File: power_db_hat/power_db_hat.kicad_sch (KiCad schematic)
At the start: 32 parts, among them J2 BAT2, J5 24V_out, J8 BAT1, U7 B2B pins

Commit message: lol
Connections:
- net +3V3: now also U7.5c, U7.7c; no longer U7.8c
- net GND: now also U7.11c, U7.9c; no longer U7.10c, U7.12c
- net LED_PWM_1: now also U7.12c; no longer U7.9c
- net LED_PWM_2: now also U7.10c; no longer U7.11c
- net MOTOR_1_A: now also U7.8c; no longer U7.1c
- net MOTOR_1_B: now also U7.6c; no longer U7.3c
- net MOTOR_2_A: now also U7.4c; no longer U7.5c
- net MOTOR_2_B: now also U7.2c; no longer U7.7c
- net SERVO_1: now also U7.3c; no longer U7.2c
- net SERVO_2: now also U7.1c; no longer U7.4c
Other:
- moved on the sheet: C45, C46, U7C

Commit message: damo was here
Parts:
- removed C2, C4, C49: 100nF, Capacitor_SMD:C_0603_1608Metric_Pad1.08x0.95mm_HandSolder, symbol Device:C
- removed C50: 22uF, Capacitor_SMD:C_0603_1608Metric_Pad1.08x0.95mm_HandSolder, symbol Device:C
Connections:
- net GND: no longer U7.11c
- net I2C_SCL: now also U7.11b; no longer U7.12b
- net I2C_SDA: now also U7.12b; no longer U7.11b
- net IND: now also U7.11c
- net LED_PWM_1: now also U7.10c; no longer U7.12c
- net LED_PWM_2: now also U7.12c; no longer U7.10c
- net MOTOR_1_A: now also U7.4c; no longer U7.8c
- net MOTOR_1_B: now also U7.2c; no longer U7.6c
- net MOTOR_2_A: now also U7.8c; no longer U7.4c
- net MOTOR_2_B: now also U7.6c; no longer U7.2c

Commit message: working on interface board
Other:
- moved on the sheet: C45, C46, U7A, U7C

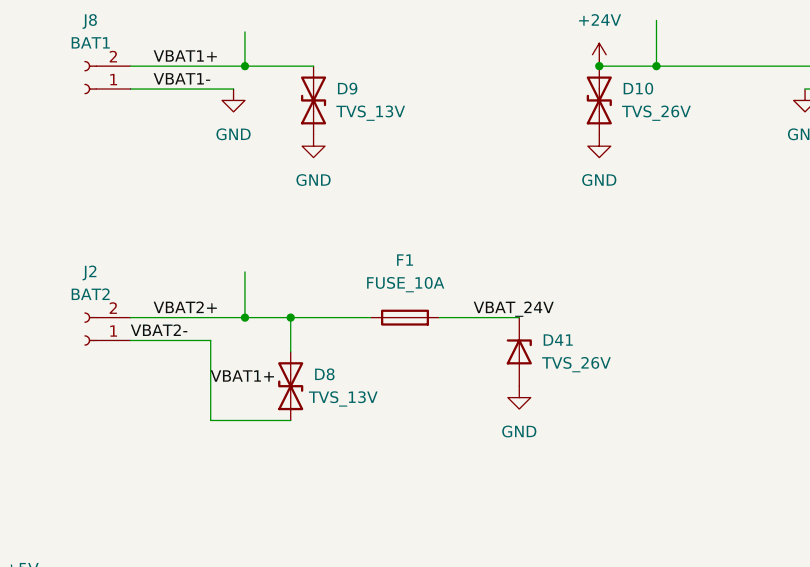
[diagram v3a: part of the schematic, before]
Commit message: updated 3d models for power
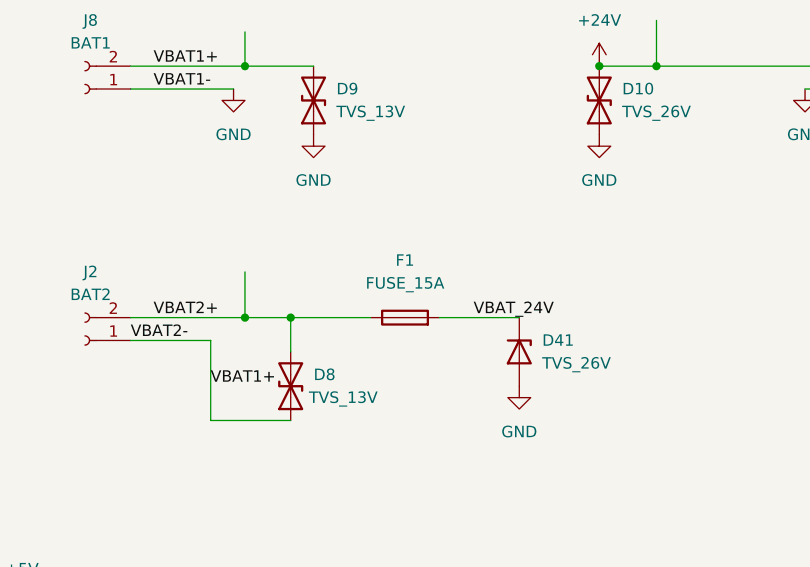
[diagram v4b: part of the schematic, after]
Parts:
- F1: value FUSE_10A -> FUSE_15A; footprint Fuse:Fuse_2512_6332Metric_Pad1.52x3.35mm_HandSolder -> Fuse:Fuse_1206_3216Metric_Pad1.42x1.75mm_HandSolder
- TP4: footprint TestPoint:TestPoint_Pad_D1.0mm -> INA3221:QFN65P400X400X100-17N-D
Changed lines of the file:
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@@
 			)
 		)
-		(property "Footprint" "TestPoint:TestPoint_Pad_D1.0mm"
+		(property "Footprint" "INA3221:QFN65P400X400X100-17N-D"
 			(at 78.74 156.21 0)
 			(hide yes)
@@
 			)
 		)
-		(property "Value" "FUSE_10A"
+		(property "Value" "FUSE_15A"
 			(at 161.29 57.15 90)
 			(show_name no)
@@
 			)
 		)
-		(property "Footprint" "Fuse:Fuse_2512_6332Metric_Pad1.52x3.35mm_HandSolder"
+		(property "Footprint" "Fuse:Fuse_1206_3216Metric_Pad1.42x1.75mm_HandSolder"
 			(at 161.29 62.738 90)
 			(hide yes)

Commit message: complete BOM
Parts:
- removed D8: TVS_13V, Diode_SMD:D_SMB_Handsoldering, symbol Device:D_TVS
- D10, D9: footprint Diode_SMD:D_SMB_Handsoldering -> Diode_SMD:D_SMA_Handsoldering
- D41: footprint Diode_SMD:D_0603_1608Metric_Pad1.05x0.95mm_HandSolder -> Diode_SMD:D_SMA_Handsoldering
- TP4: footprint INA3221:QFN65P400X400X100-17N-D -> TestPoint:TestPoint_Pad_D1.0mm
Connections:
- net VBAT2+: now also D41.1 (K)
- net VBAT_24V: no longer D41.1 (K)
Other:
- moved on the sheet: D41

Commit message: ordered
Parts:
- C46, C48: footprint Capacitor_SMD:C_0603_1608Metric_Pad1.08x0.95mm_HandSolder -> Capacitor_SMD:C_0805_2012Metric
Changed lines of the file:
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@@
 			)
 		)
-		(property "Footprint" "Capacitor_SMD:C_0603_1608Metric_Pad1.08x0.95mm_HandSolder"
+		(property "Footprint" "Capacitor_SMD:C_0805_2012Metric"
 			(at 268.9352 124.46 0)
 			(hide yes)
@@
 			)
 		)
-		(property "Footprint" "Capacitor_SMD:C_0603_1608Metric_Pad1.08x0.95mm_HandSolder"
+		(property "Footprint" "Capacitor_SMD:C_0805_2012Metric"
 			(at 201.6252 114.3 0)
 			(hide yes)

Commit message: bringup updates
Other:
- note added: "SDA AND SCL FLIPPED IN FIRST REVISION"
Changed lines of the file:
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@@
 		(date "15 nov 2012")
+	)
+	(text "SDA AND SCL FLIPPED IN FIRST REVISION\n"
+		(exclude_from_sim no)
+		(at 46.99 120.142 0)
+		(effects
+			(font
+				(size 1.27 1.27)
+			)
+		)
 	)
 	(text "TODO \ncheck available components in lab\n"
@@
 		)
 	)
-	(label "I2C_SCL"
-		(at 67.31 110.49 180)
-		(effects
-			(font
-				(size 1.27 1.27)
-			)
-			(justify right bottom)
-		)
-	)
 	(label "LED_PWM_1"
 		(at 236.22 119.38 180)
@@
 		)
 	)
+	(label "I2C_SCL"
+		(at 67.31 107.95 180)
+		(effects
+			(font
+				(size 1.27 1.27)
+			)
+			(justify right bottom)
+		)
+	)
 	(label "MOTOR_2_A"
 		(at 241.3 59.69 180)
@@
 		)
 	)
+	(label "I2C_SDA"
+		(at 67.31 110.49 180)
+		(effects
+			(font
+				(size 1.27 1.27)
+			)
+			(justify right bottom)
+		)
+	)
 	(label "VBAT2-"
 		(at 130.81 63.5 0)
@@
 		)
 	)
-	(label "I2C_SDA"
-		(at 67.31 107.95 180)
-		(effects
-			(font
-				(size 1.27 1.27)
-			)
-			(justify right bottom)
-		)
-	)

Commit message: update
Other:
- sheet expansion ports: added I2C_SCL, I2C_SDA, ~{LDAC}; removed LED_PWM_1, LED_PWM_2
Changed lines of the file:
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@@
 	(wire
 		(pts
-			(xy 245.11 49.53) (xy 248.92 49.53)
-		)
-		(stroke
-			(width 0)
-			(type default)
-		)
-	)
-	(wire
-		(pts
 			(xy 156.21 154.94) (xy 156.21 162.56)
 		)
@@
 	(wire
 		(pts
+			(xy 243.84 72.39) (xy 248.92 72.39)
+		)
+		(stroke
+			(width 0)
+			(type default)
+		)
+	)
+	(wire
+		(pts
 			(xy 67.31 107.95) (xy 69.85 107.95)
 		)
@@
 	(wire
 		(pts
-			(xy 245.11 46.99) (xy 248.92 46.99)
-		)
-		(stroke
-			(width 0)
-			(type default)
-		)
-	)
-	(wire
-		(pts
 			(xy 46.99 151.13) (xy 46.99 156.21)
 		)
@@
 	(wire
 		(pts
+			(xy 245.11 74.93) (xy 248.92 74.93)
+		)
+		(stroke
+			(width 0)
+			(type default)
+		)
+	)
+	(wire
+		(pts
+			(xy 243.84 69.85) (xy 248.92 69.85)
+		)
+		(stroke
+			(width 0)
+			(type default)
+		)
+	)
+	(wire
+		(pts
 			(xy 275.59 116.84) (xy 267.97 116.84)
 		)
@@
 		)
 	)
+	(label "LED_PWM_1"
+		(at 245.11 74.93 180)
+		(effects
+			(font
+				(size 1.27 1.27)
+			)
+			(justify right bottom)
+		)
+	)
 	(label "I2C_SCL"
 		(at 186.69 118.11 0)
@@
 		)
 	)
-	(label "LED_PWM_2"
-		(at 245.11 46.99 180)
-		(effects
-			(font
-				(size 1.27 1.27)
-			)
-			(justify right bottom)
-		)
-	)
 	(label "VBAT1+"
 		(at 133.35 33.02 0)
@@
 		)
 	)
-	(label "LED_PWM_1"
-		(at 245.11 49.53 180)
+	(label "I2C_SDA"
+		(at 243.84 72.39 180)
 		(effects
 			(font
@@
 		)
 	)
+	(label "I2C_SCL"
+		(at 243.84 69.85 180)
+		(effects
+			(font
+				(size 1.27 1.27)
+			)
+			(justify right bottom)
+		)
+	)
 	(label "IND"
 		(at 87.63 156.21 0)
@@
 	(sheet
 		(at 248.92 38.735)
-		(size 12.7 32.385)
+		(size 20.955 41.275)
 		(exclude_from_sim no)
 		(in_bom yes)
@@
 		)
 		(property "Sheetfile" "servos+gpio.kicad_sch"
-			(at 248.92 71.7046 0)
+			(at 248.92 80.5946 0)
 			(show_name no)
 			(do_not_autoplace no)
@@
 			)
 		)
-		(pin "LED_PWM_1" input
-			(at 248.92 49.53 180)
+		(pin "MOTOR_1_A" input
+			(at 248.92 54.61 180)
 			(effects
 				(font
@@
 			)
 		)
-		(pin "LED_PWM_2" input
-			(at 248.92 46.99 180)
+		(pin "MOTOR_1_B" input
+			(at 248.92 57.15 180)
 			(effects
 				(font
@@
 			)
 		)
-		(pin "MOTOR_1_A" input
-			(at 248.92 54.61 180)
+		(pin "MOTOR_2_A" input
+			(at 248.92 59.69 180)
 			(effects
 				(font
@@
 			)
 		)
-		(pin "MOTOR_1_B" input
-			(at 248.92 57.15 180)
+		(pin "MOTOR_2_B" input
+			(at 248.92 62.23 180)
 			(effects
 				(font
@@
 			)
 		)
-		(pin "MOTOR_2_A" input
-			(at 248.92 59.69 180)
+		(pin "PWM_1" input
+			(at 248.92 40.64 180)
 			(effects
 				(font
@@
 			)
 		)
-		(pin "MOTOR_2_B" input
-			(at 248.92 62.23 180)
+		(pin "PWM_2" input
+			(at 248.92 43.18 180)
 			(effects
 				(font
@@
 			)
 		)
-		(pin "PWM_1" input
-			(at 248.92 40.64 180)
+		(pin "I2C_SCL" input
+			(at 248.92 69.85 180)
 			(effects
 				(font
@@
 			)
 		)
-		(pin "PWM_2" input
-			(at 248.92 43.18 180)
+		(pin "I2C_SDA" input
+			(at 248.92 72.39 180)
+			(effects
+				(font
+					(size 1.27 1.27)
+				)
+				(justify left)
+			)
+		)
+		(pin "~{LDAC}" input
+			(at 248.92 74.93 180)
 			(effects
 				(font
